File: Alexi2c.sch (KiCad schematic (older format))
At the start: 26 parts, among them J1 Conn_01x04, J10 Conn_01x01, J11 Conn_01x09, J12 Conn_01x02, J13 Conn_01x02, J2 Conn_02x03_Counter_Clockwise, J3 Conn_01x02, J4 Conn_01x10, J5 Conn_01x10, J6 Conn_01x09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

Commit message: Readme cleanup
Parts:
- J12, J13: footprint conn_kk100:kk100_22-23-2021 -> Pin_Headers:Pin_Header_Straight_1x02_Pitch2.54mm
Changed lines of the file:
@@
 F 0 "J12" H 6850 5900 50  0000 C CNN
 F 1 "Conn_01x02" H 6850 5600 50  0000 C CNN
-F 2 "conn_kk100:kk100_22-23-2021" H 6850 5800 50  0001 C CNN
+F 2 "Pin_Headers:Pin_Header_Straight_1x02_Pitch2.54mm" H 6850 5800 50  0001 C CNN
 F 3 "" H 6850 5800 50  0001 C CNN
 	1    6850 5800
@@
 F 0 "J13" H 7250 6050 50  0000 C CNN
 F 1 "Conn_01x02" H 7250 5750 50  0000 C CNN
-F 2 "conn_kk100:kk100_22-23-2021" H 7250 5950 50  0001 C CNN
+F 2 "Pin_Headers:Pin_Header_Straight_1x02_Pitch2.54mm" H 7250 5950 50  0001 C CNN
 F 3 "" H 7250 5950 50  0001 C CNN
 	1    7250 5950

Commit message: new I2C decoder module
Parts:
- removed J2: Conn_02x03_Counter_Clockwise, Pin_Headers:Pin_Header_Straight_2x03_Pitch2.54mm, symbol Conn_02x03_Counter_Clockwise
- added J2: Conn_02x03_Odd_Even, Pin_Headers:Pin_Header_Straight_2x03_Pitch2.54mm, symbol Conn_02x03_Odd_Even
- U2: footprint Housings_SOIC:SOIC-24W_7.5x15.4mm_Pitch1.27mm -> Housings_SSOP:TSSOP-24_4.4x7.8mm_Pitch0.65mm
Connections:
- no-connect marks 0 -> 1
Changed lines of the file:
@@
 F 0 "U2" H 4150 5100 50  0000 C CNN
 F 1 "TCA9555PWR" H 4600 4150 50  0000 C CNN
-F 2 "Housings_SOIC:SOIC-24W_7.5x15.4mm_Pitch1.27mm" H 5650 3150 50  0001 C CNN
+F 2 "Housings_SSOP:TSSOP-24_4.4x7.8mm_Pitch0.65mm" H 5650 3150 50  0001 C CNN
 F 3 "" H 4100 5050 50  0001 C CNN
 	1    4600 4150
@@
 Red Pitaya I/O interface (I2C) for Alexiares & Penelope filter set\n
 $Comp
-L Conn_02x03_Counter_Clockwise J2
-U 1 1 59F8B716
-P 3050 4850
-F 0 "J2" H 3100 5050 50  0000 C CNN
-F 1 "Conn_02x03_Counter_Clockwise" H 3100 4650 50  0000 C CNN
-F 2 "Pin_Headers:Pin_Header_Straight_2x03_Pitch2.54mm" H 3050 4850 50  0001 C CNN
-F 3 "" H 3050 4850 50  0001 C CNN
-	1    3050 4850
-	1    0    0    -1
-$EndComp
-$Comp
 L Conn_01x01 J7
 U 1 1 59F97D13
@@
 	-1   0    0    1
 $EndComp
+$Comp
+L Conn_02x03_Odd_Even J2
+U 1 1 5A171BE9
+P 3050 4850
+F 0 "J2" H 3100 5050 50  0000 C CNN
+F 1 "Conn_02x03_Odd_Even" H 3100 4650 50  0000 C CNN
+F 2 "Pin_Headers:Pin_Header_Straight_2x03_Pitch2.54mm" H 3050 4850 50  0001 C CNN
+F 3 "" H 3050 4850 50  0001 C CNN
+	1    3050 4850
+	1    0    0    -1
+$EndComp
+NoConn ~ 3900 3550
 $EndSCHEMATC

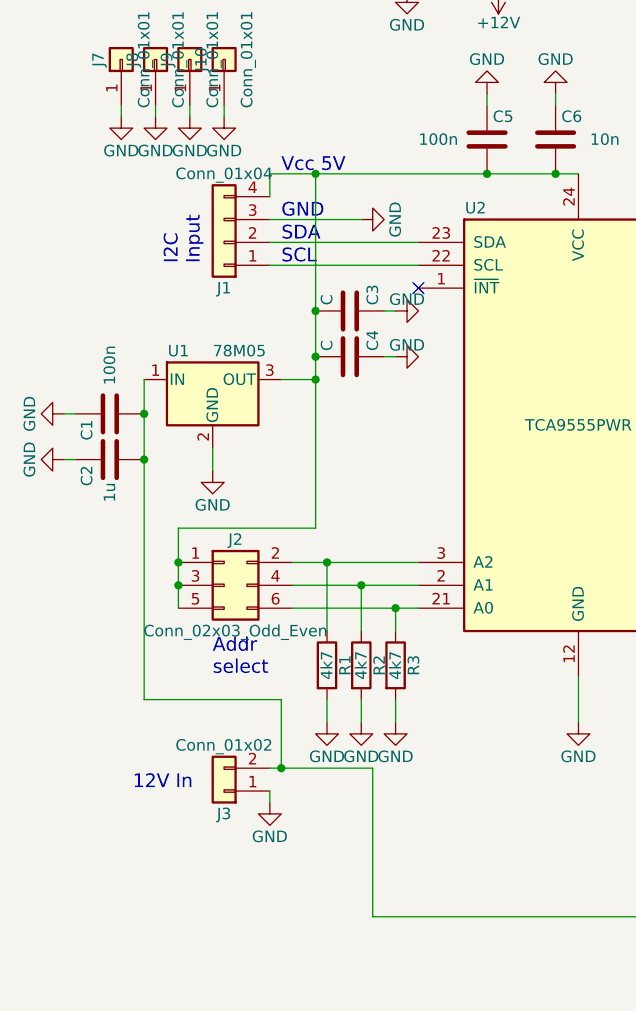
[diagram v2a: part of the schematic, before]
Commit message: added protec. diode, I2C Pull-up, I2C Vdd strap
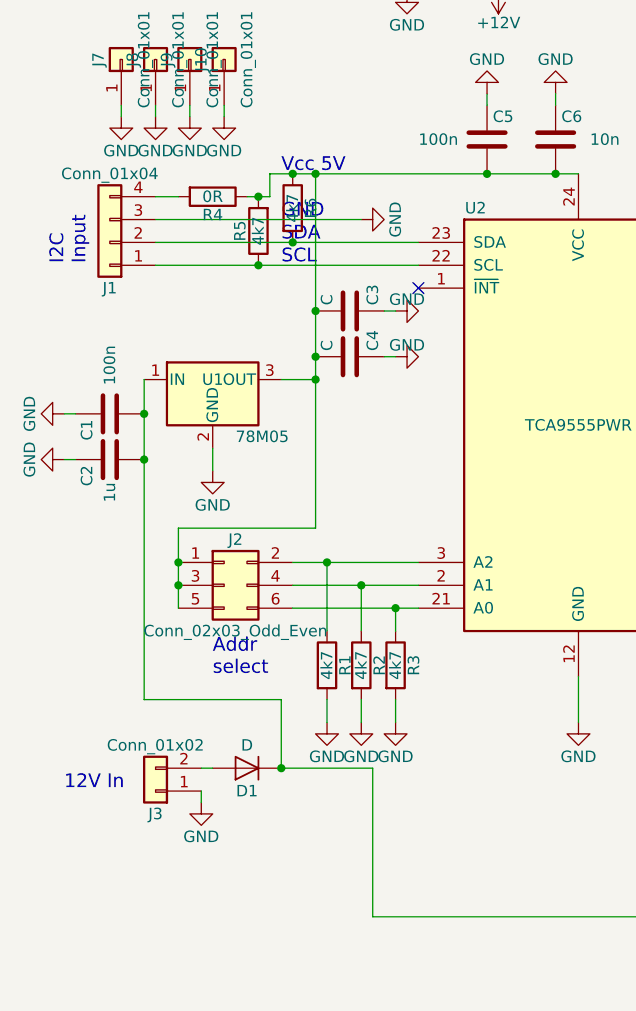
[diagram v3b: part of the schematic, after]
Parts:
- added D1: D, Diodes_SMD:D_2010, symbol D
- added R4: 0R, Resistors_SMD:R_0805_HandSoldering, symbol R
- added R5, R6: 4k7, Resistors_SMD:R_0805_HandSoldering, symbol R
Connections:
- net at J1.1 (Pin_1), U2.22 (SCL): now also R5.1
- net at J1.2 (Pin_2), U2.23 (SDA): now also R6.2
- net at C3.2, C4.2, C5.2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: now also R4.1, R5.2, R6.1; no longer J1.4 (Pin_4)
- net at C1.2, C2.2, J12.2 (Pin_2)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: now also D1.1 (K); no longer J3.2 (Pin_2)
- new net: D1.2 (A), J3.2 (Pin_2)
- new net: J1.4 (Pin_4), R4.2
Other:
- moved on the sheet: J1, J3
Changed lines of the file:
@@
 L Conn_01x02 J3
 U 1 1 59CE6CD4
-P 3050 5750
-F 0 "J3" H 3050 5850 50  0000 C CNN
-F 1 "Conn_01x02" H 3050 5550 50  0000 C CNN
-F 2 "conn_kk100:kk100_22-23-2021" H 3050 5750 50  0001 C CNN
-F 3 "" H 3050 5750 50  0001 C CNN
-	1    3050 5750
+P 2750 5750
+F 0 "J3" H 2750 5850 50  0000 C CNN
+F 1 "Conn_01x02" H 2750 5550 50  0000 C CNN
+F 2 "conn_kk100:kk100_22-23-2021" H 2750 5750 50  0001 C CNN
+F 3 "" H 2750 5750 50  0001 C CNN
+	1    2750 5750
 	-1   0    0    1
 $EndComp
@@
 L GND #PWR012
 U 1 1 59CE6DC7
-P 3250 5800
-F 0 "#PWR012" H 3250 5550 50  0001 C CNN
-F 1 "GND" H 3250 5650 50  0000 C CNN
-F 2 "" H 3250 5800 50  0001 C CNN
-F 3 "" H 3250 5800 50  0001 C CNN
-	1    3250 5800
+P 2950 5800
+F 0 "#PWR012" H 2950 5550 50  0001 C CNN
+F 1 "GND" H 2950 5650 50  0000 C CNN
+F 2 "" H 2950 5800 50  0001 C CNN
+F 3 "" H 2950 5800 50  0001 C CNN
+	1    2950 5800
 	-1   0    0    -1
 $EndComp
-Text Notes 2650 5750 0    60   ~ 0
+Text Notes 2350 5750 0    60   ~ 0
 12V In
 Text Notes 3000 5250 0    60   ~ 0
 Addr\nselect
-Text Notes 2950 3450 1    60   ~ 0
+Text Notes 2450 3450 1    60   ~ 0
 I2C \nInput
 Wire Wire Line
-	3250 3450 3900 3450
-Wire Wire Line
-	3250 3350 3900 3350
-Wire Wire Line
-	3250 3250 3650 3250
+	2750 3450 3900 3450
+Wire Wire Line
+	2750 3350 3900 3350
+Wire Wire Line
+	2750 3250 3650 3250
 Wire Wire Line
 	3350 4950 3900 4950
@@
 	7200 3950 7200 4000
 Wire Wire Line
-	3250 5750 3250 5800
+	2950 5750 2950 5800
 $Comp
 L L7805 U1
 U 1 1 59CE7A6C
 P 3000 3950
-F 0 "U1" H 2850 4075 50  0000 C CNN
-F 1 "78M05" H 3000 4075 50  0000 L CNN
+F 0 "U1" H 3000 3950 50  0000 C CNN
+F 1 "78M05" H 3100 3700 50  0000 L CNN
 F 2 "TO_SOT_Packages_SMD:TO-252-2" H 3025 3800 50  0001 L CIN
 F 3 "" H 3000 3900 50  0001 C CNN
@@
 Wire Wire Line
 	5300 5350 5300 5400
-Wire Wire Line
-	3250 5650 3700 5650
 $Comp
 L Conn_01x02 J12
@@
 L Conn_01x04 J1
 U 1 1 59F9E2B5
-P 3050 3350
-F 0 "J1" H 3050 3550 50  0000 C CNN
-F 1 "Conn_01x04" H 3050 3050 50  0000 C CNN
-F 2 "conn_kk100:kk100_22-23-2041" H 3050 3350 50  0001 C CNN
-F 3 "" H 3050 3350 50  0001 C CNN
-	1    3050 3350
+P 2550 3350
+F 0 "J1" H 2550 3550 50  0000 C CNN
+F 1 "Conn_01x04" H 2550 3050 50  0000 C CNN
+F 2 "conn_kk100:kk100_22-23-2041" H 2550 3350 50  0001 C CNN
+F 3 "" H 2550 3350 50  0001 C CNN
+	1    2550 3350
 	-1   0    0    1
 $EndComp
@@
 $EndComp
 NoConn ~ 3900 3550
+Wire Wire Line
+	3700 5650 3300 5650
+$Comp
+L D D1
+U 1 1 5A350050
+P 3150 5650
+F 0 "D1" H 3150 5750 50  0000 C CNN
+F 1 "D" H 3150 5550 50  0000 C CNN
+F 2 "Diodes_SMD:D_2010" H 3150 5650 50  0001 C CNN
+F 3 "" H 3150 5650 50  0001 C CNN
+	1    3150 5650
+	-1   0    0    1
+$EndComp
+Wire Wire Line
+	2950 5650 3000 5650
+$Comp
+L R R4
+U 1 1 5A3CF7F2
+P 3000 3150
+F 0 "R4" V 3080 3150 50  0000 C CNN
+F 1 "0R" V 3000 3150 50  0000 C CNN
+F 2 "Resistors_SMD:R_0805_HandSoldering" V 2930 3150 50  0001 C CNN
+F 3 "" H 3000 3150 50  0001 C CNN
+	1    3000 3150
+	0    1    1    0
+$EndComp
+Wire Wire Line
+	3250 3150 3150 3150
+Wire Wire Line
+	2850 3150 2750 3150
+$Comp
+L R R5
+U 1 1 5A3D00FE
+P 3200 3300
+F 0 "R5" V 3280 3300 50  0000 C CNN
+F 1 "4k7" V 3200 3300 50  0000 C CNN
+F 2 "Resistors_SMD:R_0805_HandSoldering" V 3130 3300 50  0001 C CNN
+F 3 "" H 3200 3300 50  0001 C CNN
+	1    3200 3300
+	-1   0    0    1
+$EndComp
+$Comp
+L R R6
+U 1 1 5A3D03AB
+P 3350 3200
+F 0 "R6" V 3430 3200 50  0000 C CNN
+F 1 "4k7" V 3350 3200 50  0000 C CNN
+F 2 "Resistors_SMD:R_0805_HandSoldering" V 3280 3200 50  0001 C CNN
+F 3 "" H 3350 3200 50  0001 C CNN
+	1    3350 3200
+	1    0    0    -1
+$EndComp
+Connection ~ 3200 3450
+Connection ~ 3200 3150
+Connection ~ 3350 3050
+Connection ~ 3350 3350
 $EndSCHEMATC

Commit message: image and BOM added, minor changes
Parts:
- removed C1: 100n, Capacitors_SMD:C_0805_HandSoldering, symbol C
- removed C2: 1u, Capacitors_SMD:C_0805_HandSoldering, symbol C
- removed C3, C4: C, Capacitors_SMD:C_0805_HandSoldering, symbol C
- removed U1: 78M05, TO_SOT_Packages_SMD:TO-252-2, symbol L7805
- added R7: 4k7, Resistors_SMD:R_0805_HandSoldering, symbol R
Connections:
- net at U2.1 (~INT): now also R7.2
- net at C5.2, C6.2, J2.1 (Pin_1)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: now also R7.1
- no-connect marks 1 -> 0
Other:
- note added: "Com+"
- note removed: "12Vcc"
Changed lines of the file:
@@
 L GND #PWR01
 U 1 1 59CE4270
-P 3650 3250
-F 0 "#PWR01" H 3650 3000 50  0001 C CNN
-F 1 "GND" H 3650 3100 50  0000 C CNN
-F 2 "" H 3650 3250 50  0001 C CNN
-F 3 "" H 3650 3250 50  0001 C CNN
-	1    3650 3250
+P 2800 3250
+F 0 "#PWR01" H 2800 3000 50  0001 C CNN
+F 1 "GND" H 2800 3250 50  0000 C CNN
+F 2 "" H 2800 3250 50  0001 C CNN
+F 3 "" H 2800 3250 50  0001 C CNN
+	1    2800 3250
 	0    -1   -1   0
 $EndComp
@@
 Text Notes 3000 5250 0    60   ~ 0
 Addr\nselect
-Text Notes 2450 3450 1    60   ~ 0
+Text Notes 2100 3400 1    60   ~ 0
 I2C \nInput
 Wire Wire Line
@@
 Wire Wire Line
 	2750 3350 3900 3350
-Wire Wire Line
-	2750 3250 3650 3250
 Wire Wire Line
 	3350 4950 3900 4950
@@
 Wire Wire Line
 	2950 5750 2950 5800
-$Comp
-L L7805 U1
-U 1 1 59CE7A6C
-P 3000 3950
-F 0 "U1" H 3000 3950 50  0000 C CNN
-F 1 "78M05" H 3100 3700 50  0000 L CNN
-F 2 "TO_SOT_Packages_SMD:TO-252-2" H 3025 3800 50  0001 L CIN
-F 3 "" H 3000 3900 50  0001 C CNN
-	1    3000 3950
-	1    0    0    -1
-$EndComp
 Wire Wire Line
 	3250 3050 4600 3050
@@
 Connection ~ 4200 3050
 Wire Wire Line
-	3300 3950 3450 3950
-Wire Wire Line
 	3450 3050 3450 4600
 Connection ~ 3450 3050
 Wire Wire Line
 	3450 4600 2850 4600
-Connection ~ 3450 3950
-Wire Wire Line
-	2700 3950 2700 5350
-Wire Wire Line
-	2700 5350 3300 5350
-Wire Wire Line
-	3300 5350 3300 5650
-$Comp
-L C C4
-U 1 1 59CE7EEE
-P 3600 3850
-F 0 "C4" H 3625 3950 50  0000 L CNN
-F 1 "C" H 3625 3750 50  0000 L CNN
-F 2 "Capacitors_SMD:C_0805_HandSoldering" H 3638 3700 50  0001 C CNN
-F 3 "" H 3600 3850 50  0001 C CNN
-	1    3600 3850
-	0    1    -1   0
-$EndComp
-$Comp
-L GND #PWR013
-U 1 1 59CE7EF4
-P 3800 3850
-F 0 "#PWR013" H 3800 3600 50  0001 C CNN
-F 1 "GND" V 3750 3800 50  0000 C CNN
-F 2 "" H 3800 3850 50  0001 C CNN
-F 3 "" H 3800 3850 50  0001 C CNN
-	1    3800 3850
-	0    -1   1    0
-$EndComp
-$Comp
-L C C3
-U 1 1 59CE7EFA
-P 3600 3650
-F 0 "C3" H 3625 3750 50  0000 L CNN
-F 1 "C" H 3625 3550 50  0000 L CNN
-F 2 "Capacitors_SMD:C_0805_HandSoldering" H 3638 3500 50  0001 C CNN
-F 3 "" H 3600 3650 50  0001 C CNN
-	1    3600 3650
-	0    1    -1   0
-$EndComp
-$Comp
-L GND #PWR014
-U 1 1 59CE7F00
-P 3800 3650
-F 0 "#PWR014" H 3800 3400 50  0001 C CNN
-F 1 "GND" V 3750 3600 50  0000 C CNN
-F 2 "" H 3800 3650 50  0001 C CNN
-F 3 "" H 3800 3650 50  0001 C CNN
-	1    3800 3650
-	0    -1   1    0
-$EndComp
-Wire Wire Line
-	3800 3850 3750 3850
-Wire Wire Line
-	3800 3650 3750 3650
-$Comp
-L C C1
-U 1 1 59CE846C
-P 2550 4100
-F 0 "C1" H 2575 4200 50  0000 L CNN
-F 1 "100n" H 2250 4100 50  0000 L CNN
-F 2 "Capacitors_SMD:C_0805_HandSoldering" H 2588 3950 50  0001 C CNN
-F 3 "" H 2550 4100 50  0001 C CNN
-	1    2550 4100
-	0    -1   1    0
-$EndComp
-$Comp
-L GND #PWR015
-U 1 1 59CE8472
-P 2350 4100
-F 0 "#PWR015" H 2350 3850 50  0001 C CNN
-F 1 "GND" H 2350 3950 50  0000 C CNN
-F 2 "" H 2350 4100 50  0001 C CNN
-F 3 "" H 2350 4100 50  0001 C CNN
-	1    2350 4100
-	0    1    -1   0
-$EndComp
-$Comp
-L C C2
-U 1 1 59CE8478
-P 2550 4300
-F 0 "C2" H 2575 4400 50  0000 L CNN
-F 1 "1u" H 2650 4300 50  0000 L CNN
-F 2 "Capacitors_SMD:C_0805_HandSoldering" H 2588 4150 50  0001 C CNN
-F 3 "" H 2550 4300 50  0001 C CNN
-	1    2550 4300
-	0    -1   1    0
-$EndComp
-$Comp
-L GND #PWR016
-U 1 1 59CE847E
-P 2350 4300
-F 0 "#PWR016" H 2350 4050 50  0001 C CNN
-F 1 "GND" H 2350 4150 50  0000 C CNN
-F 2 "" H 2350 4300 50  0001 C CNN
-F 3 "" H 2350 4300 50  0001 C CNN
-	1    2350 4300
-	0    1    -1   0
-$EndComp
-Wire Wire Line
-	2350 4100 2400 4100
-Wire Wire Line
-	2350 4300 2400 4300
-$Comp
-L GND #PWR017
-U 1 1 59CE89E9
-P 3000 4350
-F 0 "#PWR017" H 3000 4100 50  0001 C CNN
-F 1 "GND" H 3000 4200 50  0000 C CNN
-F 2 "" H 3000 4350 50  0001 C CNN
-F 3 "" H 3000 4350 50  0001 C CNN
-	1    3000 4350
-	1    0    0    -1
-$EndComp
-Wire Wire Line
-	3000 4250 3000 4350
 Text Notes 7200 7200 0    79   ~ 0
 I2C interface \nAlexiares/Penelope/Red Pitaya/Hermes Lite\n\nF6ITU\n\n
@@
 Wire Wire Line
 	5050 3800 5050 3850
-Text Notes 3300 3350 0    60   ~ 0
+Text Notes 2300 3400 0    60   ~ 0
 SDA\n
-Text Notes 3300 3450 0    60   ~ 0
+Text Notes 2300 3500 0    60   ~ 0
 SCL\n
-Text Notes 3300 3250 0    60   ~ 0
+Text Notes 2300 3300 0    60   ~ 0
 GND\n
 Text Notes 3300 3050 0    60   ~ 0
@@
 16
 Text Notes 7500 3900 0    60   ~ 0
-12Vcc
+Com+
 Text Notes 7500 4000 0    60   ~ 0
 Gnd\n
 Text Notes 7500 5200 0    60   ~ 0
-12Vcc
+Com+
 Text Notes 7500 5300 0    60   ~ 0
 Gnd\n
@@
 LPF
 $Comp
-L GND #PWR018
+L GND #PWR013
 U 1 1 59F8B1A6
 P 5350 2100
-F 0 "#PWR018" H 5350 1850 50  0001 C CNN
+F 0 "#PWR013" H 5350 1850 50  0001 C CNN
 F 1 "GND" V 5450 2000 50  0000 C CNN
 F 2 "" H 5350 2100 50  0001 C CNN
@@
 $EndComp
 $Comp
-L GND #PWR019
+L GND #PWR014
 U 1 1 59F8B6BC
 P 5300 5350
-F 0 "#PWR019" H 5300 5100 50  0001 C CNN
+F 0 "#PWR014" H 5300 5100 50  0001 C CNN
 F 1 "GND" V 5400 5250 50  0000 C CNN
 F 2 "" H 5300 5350 50  0001 C CNN
@@
 $EndComp
 $Comp
-L GND #PWR020
+L GND #PWR015
 U 1 1 59F97ECB
 P 2600 2800
-F 0 "#PWR020" H 2600 2550 50  0001 C CNN
+F 0 "#PWR015" H 2600 2550 50  0001 C CNN
 F 1 "GND" H 2600 2650 50  0000 C CNN
 F 2 "" H 2600 2800 50  0001 C CNN
@@
 $EndComp
 $Comp
-L GND #PWR021
+L GND #PWR016
 U 1 1 59F97F7C
 P 2750 2800
-F 0 "#PWR021" H 2750 2550 50  0001 C CNN
+F 0 "#PWR016" H 2750 2550 50  0001 C CNN
 F 1 "GND" H 2750 2650 50  0000 C CNN
 F 2 "" H 2750 2800 50  0001 C CNN
@@
 $EndComp
 $Comp
-L GND #PWR022
+L GND #PWR017
 U 1 1 59F97F99
 P 2900 2800
-F 0 "#PWR022" H 2900 2550 50  0001 C CNN
+F 0 "#PWR017" H 2900 2550 50  0001 C CNN
 F 1 "GND" H 2900 2650 50  0000 C CNN
 F 2 "" H 2900 2800 50  0001 C CNN
@@
 $EndComp
 $Comp
-L GND #PWR023
+L GND #PWR018
 U 1 1 59F97F9F
 P 3050 2800
-F 0 "#PWR023" H 3050 2550 50  0001 C CNN
+F 0 "#PWR018" H 3050 2550 50  0001 C CNN
 F 1 "GND" H 3050 2650 50  0000 C CNN
 F 2 "" H 3050 2800 50  0001 C CNN
@@
 Wire Wire Line
 	3700 6300 3700 5650
-Connection ~ 3300 5650
 Connection ~ 6650 6050
 Text Notes 7600 6250 1    60   ~ 0
 ULN com. pwr
-Connection ~ 2700 4300
-Connection ~ 2700 4100
-Connection ~ 3450 3850
-Connection ~ 3450 3650
-$Comp
-L GND #PWR024
+$Comp
+L GND #PWR019
 U 1 1 59F9DAC6
 P 3850 2250
-F 0 "#PWR024" H 3850 2000 50  0001 C CNN
+F 0 "#PWR019" H 3850 2000 50  0001 C CNN
 F 1 "GND" H 3850 2100 50  0000 C CNN
 F 2 "" H 3850 2250 50  0001 C CNN
@@
 $EndComp
 $Comp
-L +12V #PWR025
+L +12V #PWR020
 U 1 1 59F9DB0E
 P 4250 2250
-F 0 "#PWR025" H 4250 2100 50  0001 C CNN
+F 0 "#PWR020" H 4250 2100 50  0001 C CNN
 F 1 "+12V" H 4250 2390 50  0000 C CNN
 F 2 "" H 4250 2250 50  0001 C CNN
@@
 $EndComp
 $Comp
-L PWR_FLAG #FLG026
+L PWR_FLAG #FLG021
 U 1 1 59F9DB56
 P 3850 2200
-F 0 "#FLG026" H 3850 2275 50  0001 C CNN
+F 0 "#FLG021" H 3850 2275 50  0001 C CNN
 F 1 "PWR_FLAG" H 3850 2350 50  0000 C CNN
 F 2 "" H 3850 2200 50  0001 C CNN
@@
 $EndComp
 $Comp
-L PWR_FLAG #FLG027
+L PWR_FLAG #FLG022
 U 1 1 59F9DC3A
 P 4250 2200
-F 0 "#FLG027" H 4250 2275 50  0001 C CNN
+F 0 "#FLG022" H 4250 2275 50  0001 C CNN
 F 1 "PWR_FLAG" H 4250 2350 50  0000 C CNN
 F 2 "" H 4250 2200 50  0001 C CNN
@@
 	1    0    0    -1
 $EndComp
-NoConn ~ 3900 3550
 Wire Wire Line
 	3700 5650 3300 5650
@@
 Connection ~ 3350 3050
 Connection ~ 3350 3350
+Wire Wire Line
+	2800 3250 2750 3250
+$Comp
+L R R7
+U 1 1 5A43DEEC
+P 3800 3400
+F 0 "R7" V 3880 3400 50  0000 C CNN
+F 1 "4k7" V 3800 3400 50  0000 C CNN
+F 2 "Resistors_SMD:R_0805_HandSoldering" V 3730 3400 50  0001 C CNN
+F 3 "" H 3800 3400 50  0001 C CNN
+	1    3800 3400
+	1    0    0    -1
+$EndComp
+Wire Wire Line
+	3900 3550 3800 3550
+Wire Wire Line
+	3800 3250 3800 3050
+Connection ~ 3800 3050
 $EndSCHEMATC

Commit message: upgrate to Kicad 5.0n, new up to date Gerber
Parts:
- C5, C6: symbol C -> Alexi2c-rescue:C
- D1: symbol D -> Alexi2c-rescue:D
- J1: symbol Conn_01x04 -> Alexi2c-rescue:Conn_01x04
- J10, J7, J8, J9: footprint Mounting_Holes:MountingHole_3.2mm_M3_ISO14580_Pad -> MountingHole:MountingHole_3.2mm_M3_ISO14580_Pad; symbol Conn_01x01 -> Alexi2c-rescue:Conn_01x01
- J11, J6: symbol Conn_01x09 -> Alexi2c-rescue:Conn_01x09
- J12, J13, J3: symbol Conn_01x02 -> Alexi2c-rescue:Conn_01x02
- J2: symbol Conn_02x03_Odd_Even -> Alexi2c-rescue:Conn_02x03_Odd_Even
- J4, J5: symbol Conn_01x10 -> Alexi2c-rescue:Conn_01x10
- R1, R2, R3, R4, R5, R6, R7: symbol R -> Alexi2c-rescue:R
- U2: symbol TCA9555PWR -> Alexi2c-rescue:TCA9555PWR
- U3, U4: symbol ULN2803A -> Alexi2c-rescue:ULN2803A
